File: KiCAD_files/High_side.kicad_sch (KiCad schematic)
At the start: 27 parts, among them U601 AMC1311BDWVR, U602 +-20A Hall, U603 MCP6486UT-E/LT, U604 MCP6486UT-E/LT

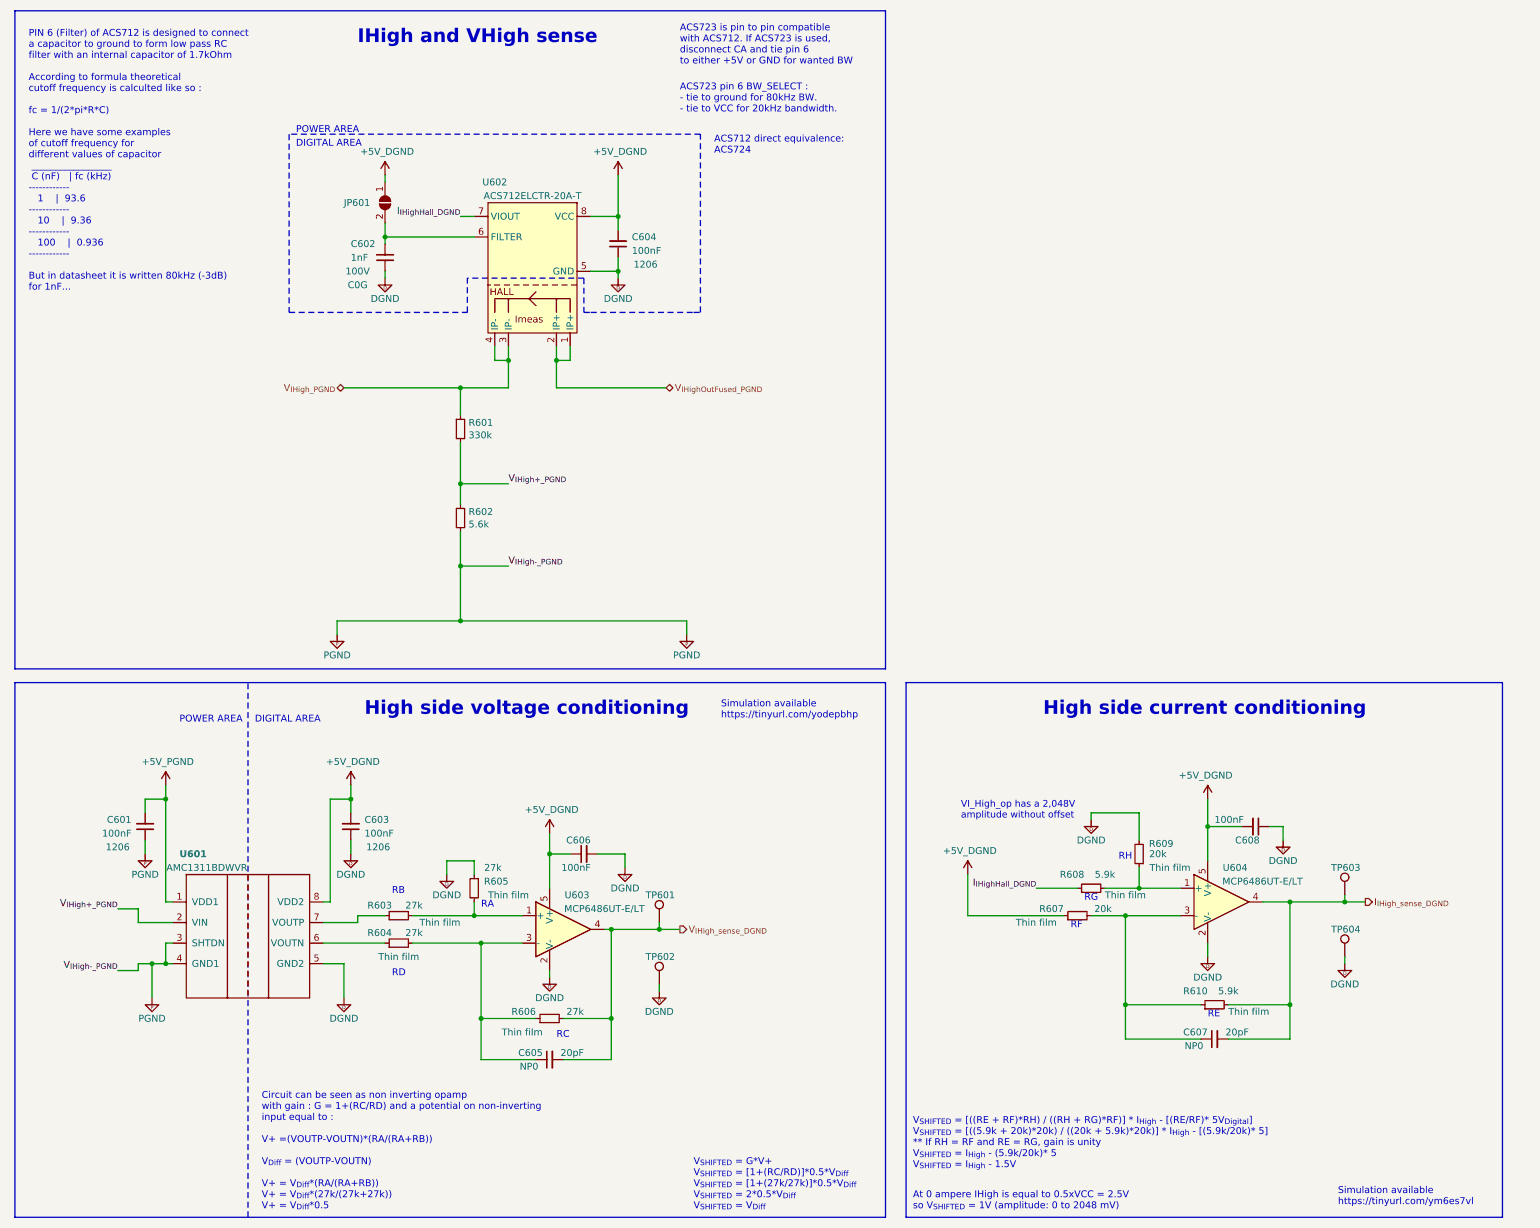
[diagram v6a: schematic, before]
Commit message: Rule zones added, DRC rules added, Added FPC connectors
Signed-off-by: Jean Alinei <jean.alinei@owntech.org>
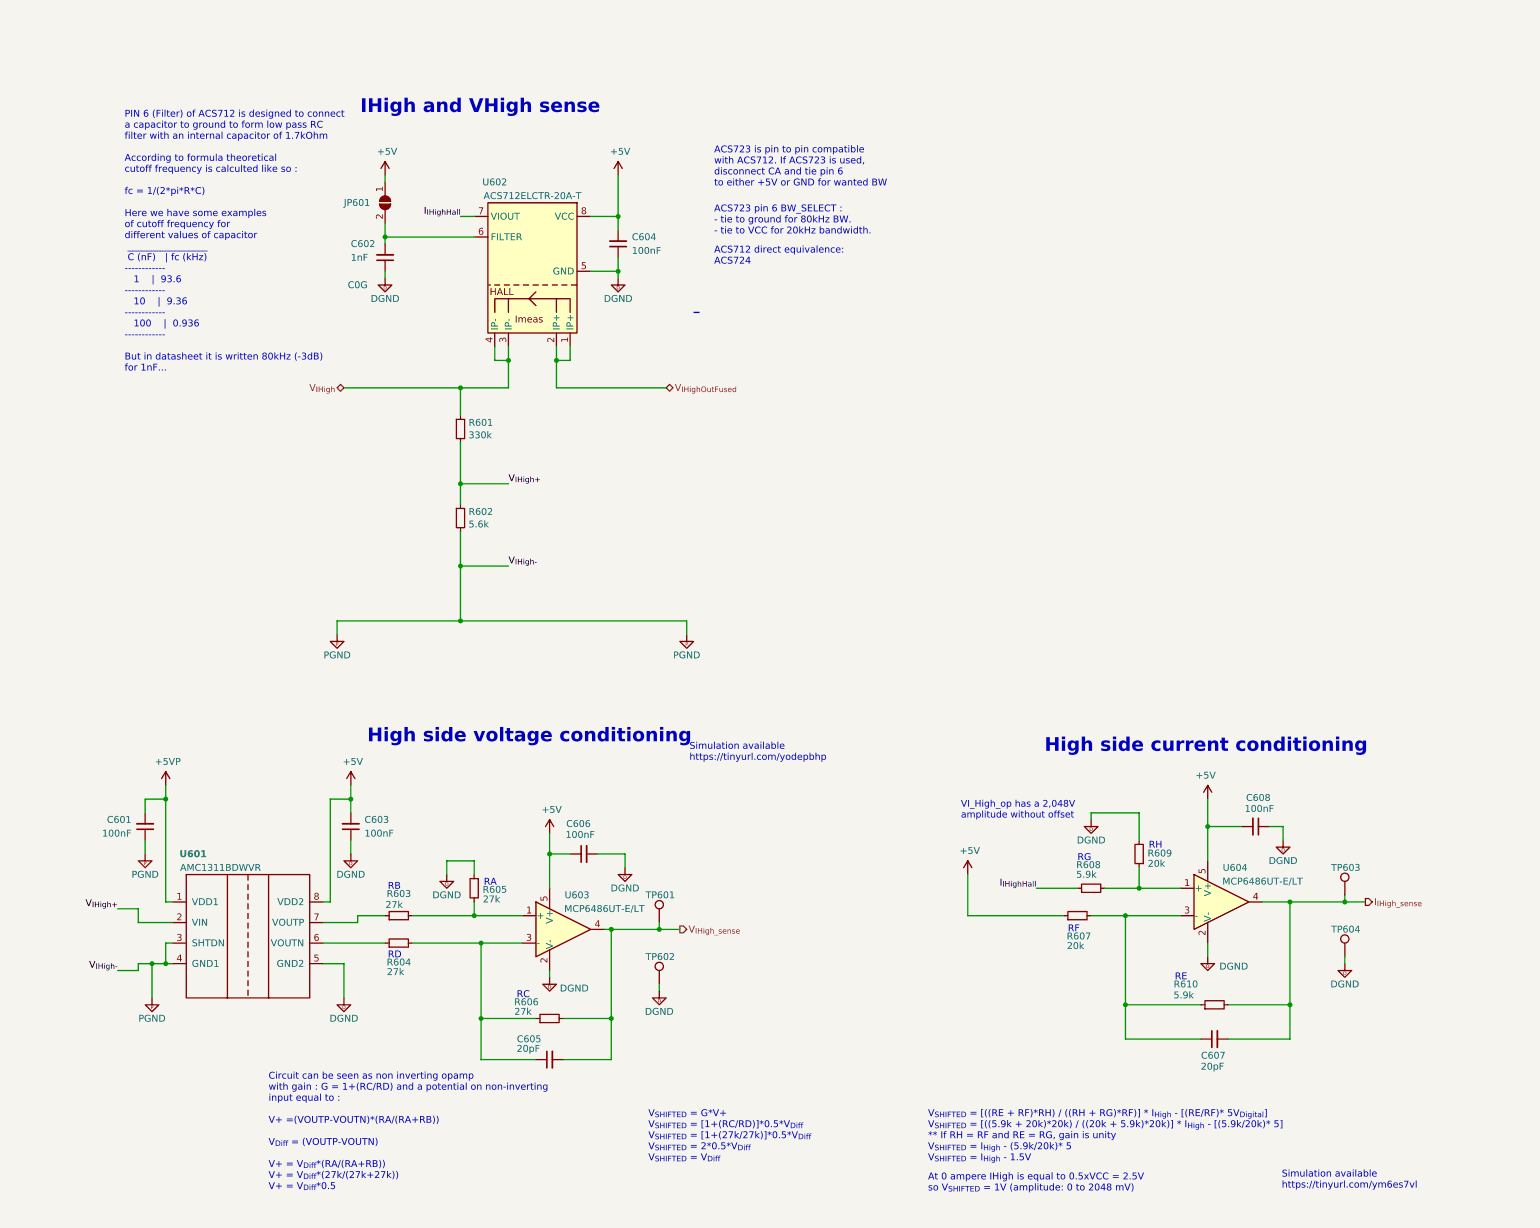
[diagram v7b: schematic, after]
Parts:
- C601, C603, C604, C606, C608: Package 1206 -> (none); Voltage 50V -> (none); Voltage_Rating (none) -> 50V
- C602: Package 0805 -> (none); Voltage 100V -> (none); Voltage_Rating (none) -> 100V
- C605, C607: Package 0805 -> (none); Voltage 50V -> (none); Voltage_Rating (none) -> 50V
- JP601, TP601, TP602, TP603, TP604: DNP x -> (none)
- R601, R602: Package 0805 -> (none); Technology Thick film -> (none)
- R603, R604, R605, R606, R607, R608, R609, R610: Package 0805 -> (none); Technology Thin film -> (none)
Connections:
- net +5V_DGND renamed +5V
- net +5V_PGND renamed +5VP
- net I_{IHighHall_DGND} renamed I_{IHighHall}
- net I_{IHigh_sense_DGND} renamed I_{IHigh_sense}
- net V_{IHigh+_PGND} renamed V_{IHigh+}
- net V_{IHighOutFused_PGND} renamed V_{IHighOutFused}
- net V_{IHigh_PGND} renamed V_{IHigh}
- net V_{IHigh_sense_DGND} renamed V_{IHigh_sense}
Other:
- note removed: "DIGITAL AREA"
- note removed: "POWER AREA"
- company: https://gitlab.laas.fr/owntech/boards/TWIST -> https://github.com/owntech-foundation/twist
- title: TWIST 1.4 -> TWIST 1.4.2
